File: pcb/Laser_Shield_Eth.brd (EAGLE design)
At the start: 68.6 x 53.3 mm, 64 parts, among them IC1 CAT811TTBI-CT3, IC11 74LVC1G14DBV, IC2 MC33269ST-3, IC3 MC33269D-3, IC4 W5100, J4 JUMPER_SOLDER_1X2, J5 JUMPER_SOLDER_1X2, J6 JUMPER_SOLDER_1X2, Q1 25MHz, Q2 MOSFET-NCHANNELSMD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

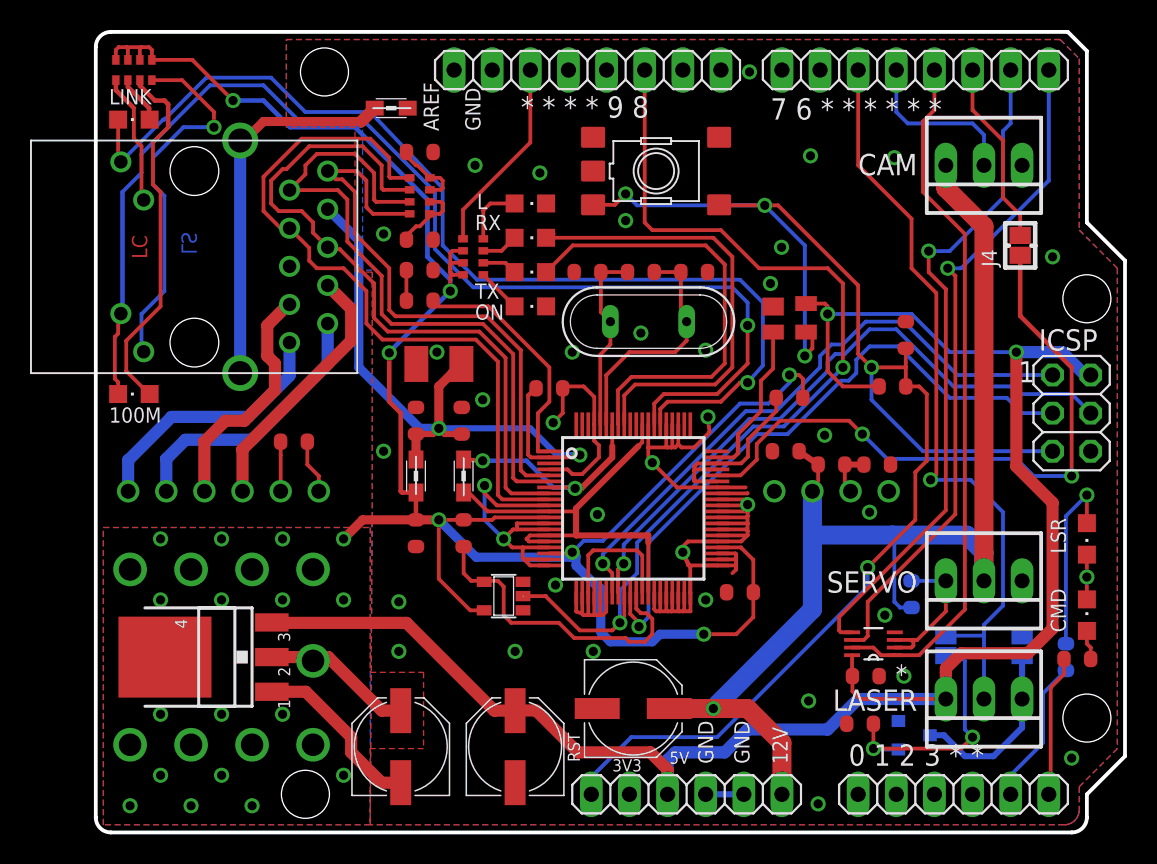
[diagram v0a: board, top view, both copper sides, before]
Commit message: pcb: more LEDS
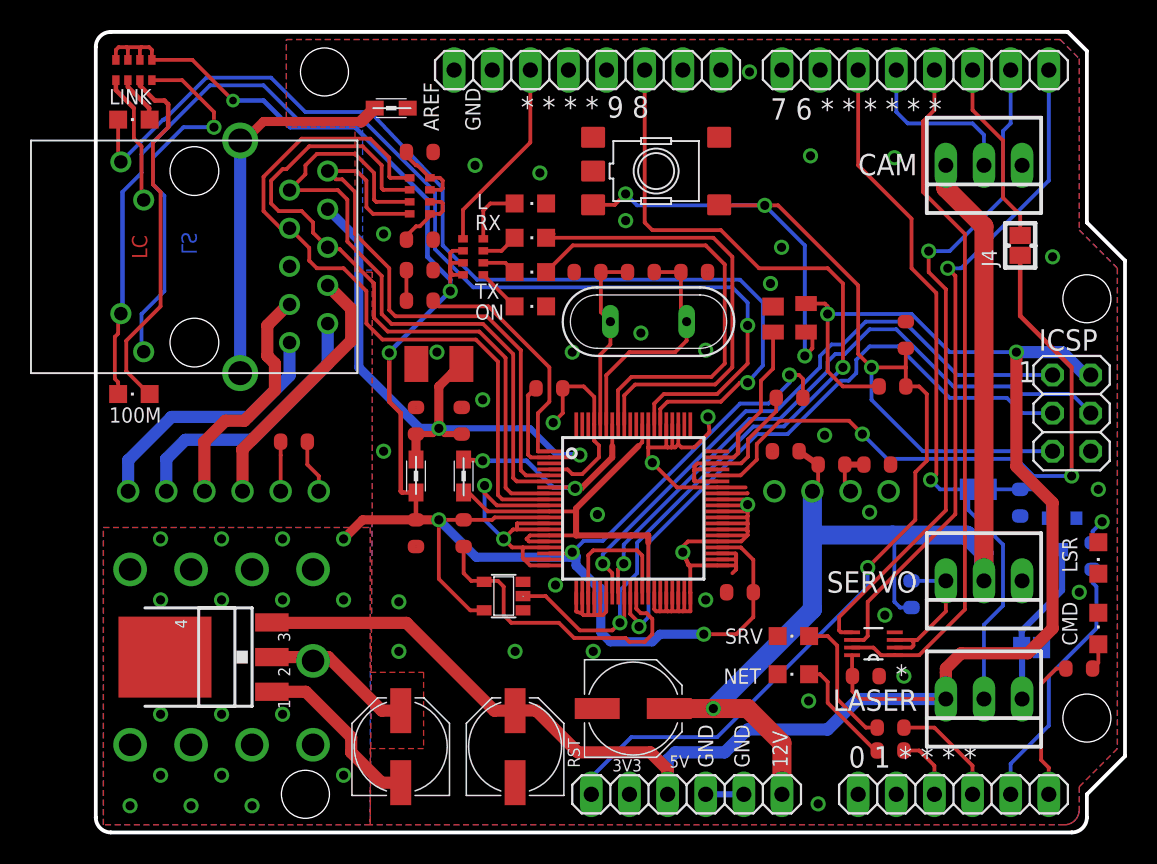
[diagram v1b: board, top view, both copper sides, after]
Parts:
- added NET, SRV: Green, led:CHIPLED_0805
- added R14, R15: 1k, SmartPrj:R0603-ROUND
- moved R13 18.2 mm to (61.6, 22.0), flipped to the bottom, turned to 90 degrees
- moved Q2 16.7 mm to (64.4, 19.9), turned to 180 degrees
- moved J6 10.6 mm to (58.8, 22.9), turned to 180 degrees
- moved R12 6.96 mm to (66.4, 18.4)
- moved LSR 1.48 mm to (66.8, 18.3)
- moved CMD 1.17 mm to (66.8, 13.6)
- moved R11 0.65 mm to (65.5, 10.9)
- moved J5 0.65 mm to (62.4, 12.3), turned to 0 degrees
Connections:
- new net N$11: R14.1, SRV.A
- new net N$12: NET.A, R15.1
- new net N$19: J2.4, R14.2
- new net N$20: J2.3, R15.2
- net GND: now also NET.C, SRV.C
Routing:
- net N$13: track 17.0 -> 5.49 mm, vias 2 -> 0
- net N$5: track 12.4 -> 1.66 mm
- net N$11: track 0.00 -> 9.15 mm
- net N$18: track 9.78 -> 17.5 mm
- net N$19: track 0.00 -> 7.53 mm
- net N$12: track 0.00 -> 7.46 mm
- net N$20: track 0.00 -> 4.36 mm
- net LASER_CTRL: track 50.9 -> 47.9 mm
- net GND: track 137.6 -> 134.6 mm
- net N$14: track 12.3 -> 11.1 mm
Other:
- board text added: "0 1 * * * *"
- board text removed: "0 1 2 3 * *"

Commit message: final pcb eth socket fixes
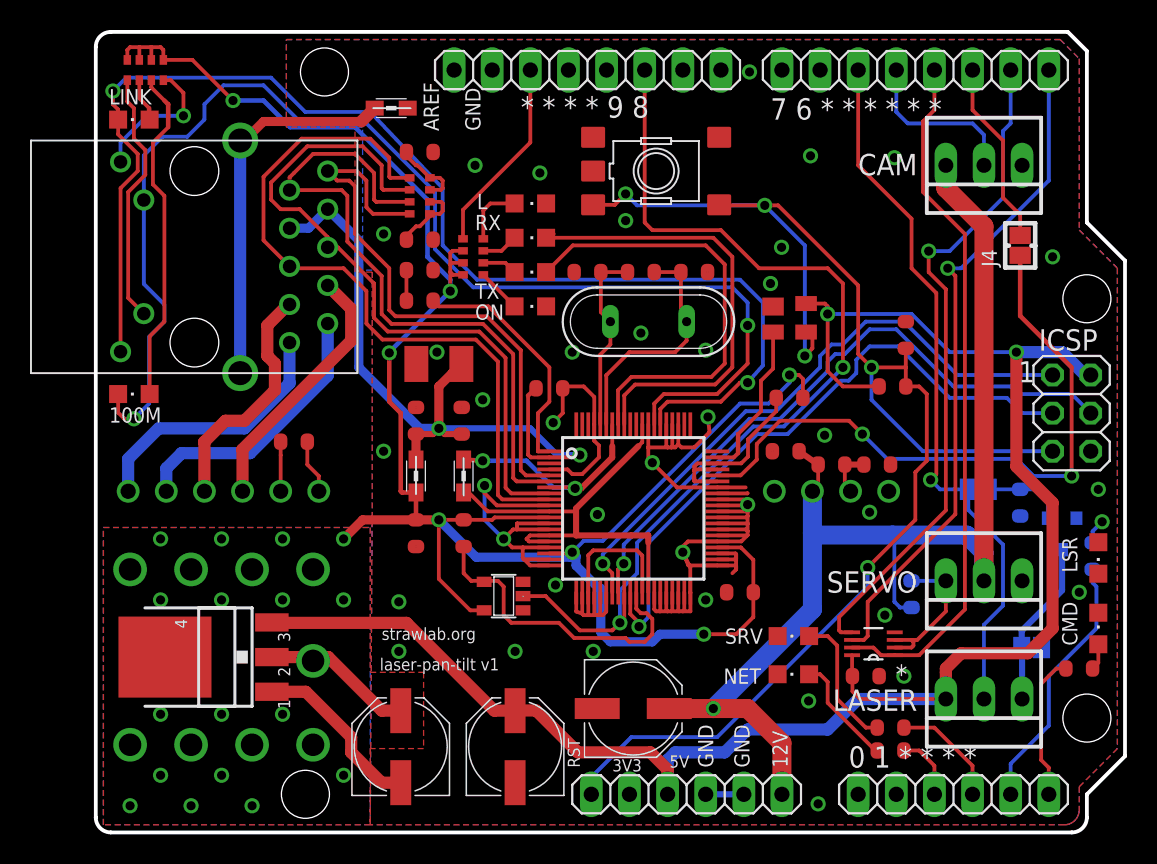
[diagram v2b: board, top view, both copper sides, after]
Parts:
- moved RN3 0.76 mm to (3.30, 50.8)
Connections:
- net +3V3A: now also U$1.R4
- net LINKLED: now also U$1.D4; no longer U$1.L4
- net N$2: now also U$1.D3; no longer U$1.L3
- net N$3: now also U$1.D1; no longer U$1.L1
- net SPDLED: now also U$1.D2; no longer U$1.L2
- net TXON: now also U$1.R6; no longer U$1.R4
- net V1+: now also U$1.R9; no longer U$1.R10
- net V1-: now also U$1.R10; no longer U$1.R9
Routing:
- net N$3: track 24.9 -> 9.44 mm
- net LINKLED: track 69.8 -> 84.4 mm, vias 1 -> 2
- net N$2: track 8.76 -> 17.0 mm
- net SPDLED: track 80.1 -> 85.2 mm, vias 1 -> 2
- net +3V3A: track 47.5 -> 50.6 mm
- net N$25: track 24.3 -> 22.6 mm
- net +3V3: track 149.8 -> 148.4 mm
- net V1+: track 17.4 -> 18.3 mm
- net SH: track 26.0 -> 25.4 mm
- net TXON: track 48.9 -> 49.5 mm
- net V1-: track 18.2 -> 17.7 mm
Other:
- board text added: "laser-pan-tilt v1"
- board text added: "strawlab.org"
- board text removed: "LC"
- board text removed: "LS"
